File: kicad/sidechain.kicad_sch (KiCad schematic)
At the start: 30 parts, among them SW2 INT/EXT, SW3 HPF DEFEAT, SW4 LINK, U3 NE5532, U4 NE5532, U6 NE5532

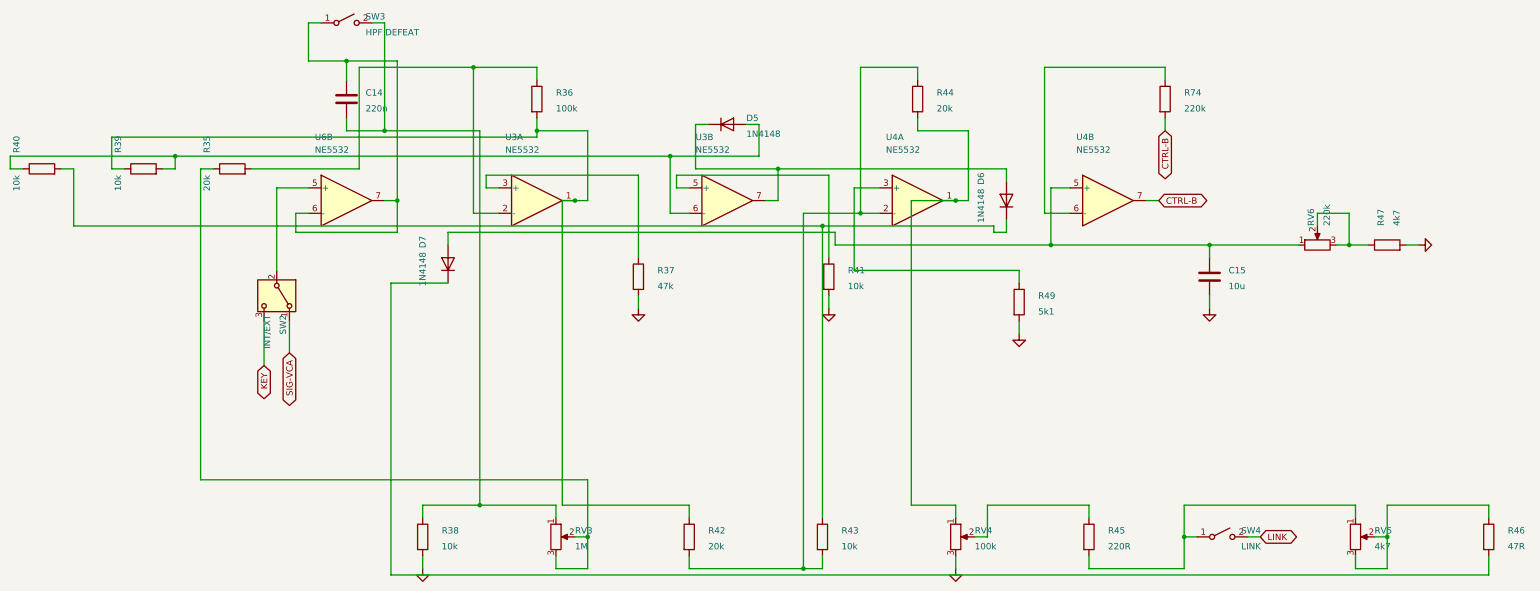
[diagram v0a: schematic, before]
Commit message: Add power shtuff and meters to big boy schematic
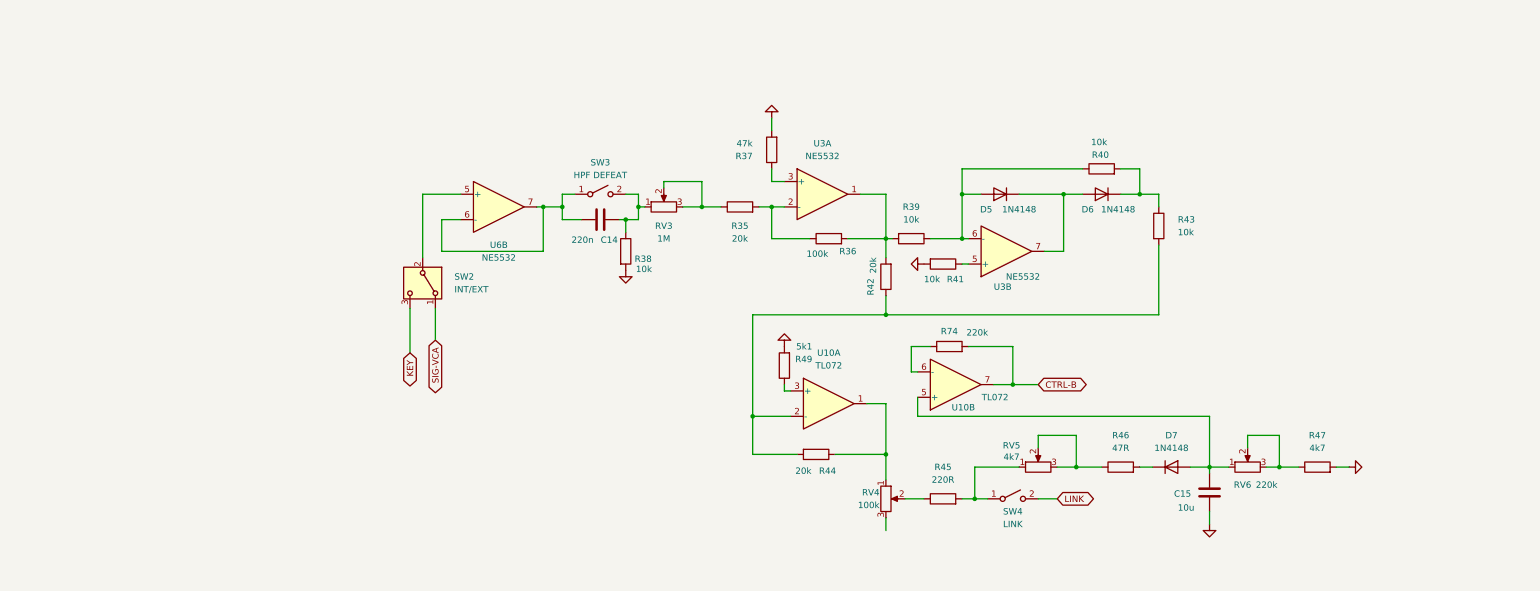
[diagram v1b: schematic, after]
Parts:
- removed U4: NE5532, Package_DIP:DIP-8_W7.62mm, symbol Amplifier_Operational:NE5532
- added U10: TL072, Package_DIP:DIP-8_W7.62mm, symbol Amplifier_Operational:NE5532
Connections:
- net AGND: no longer RV4.3
- net CTRL-B: now also U10.7
- net at C15.1, D7.2 (A), RV6.1: now also U10.5 (+)
- net at R49.1: now also U10.3 (+)
- net at R36.2, U3.1: now also R39.2, R42.2; no longer R39.1, R42.1
- net at R74.1: now also U10.6 (-)
- net at RV4.1: now also R44.1, U10.1; no longer R44.2
- net at D5.2 (A), R40.1, U3.6 (-): now also R39.1; no longer R39.2
- new net: R42.1, R43.2, R44.2, U10.2 (-)

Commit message: Add reorganised schematic to split files.
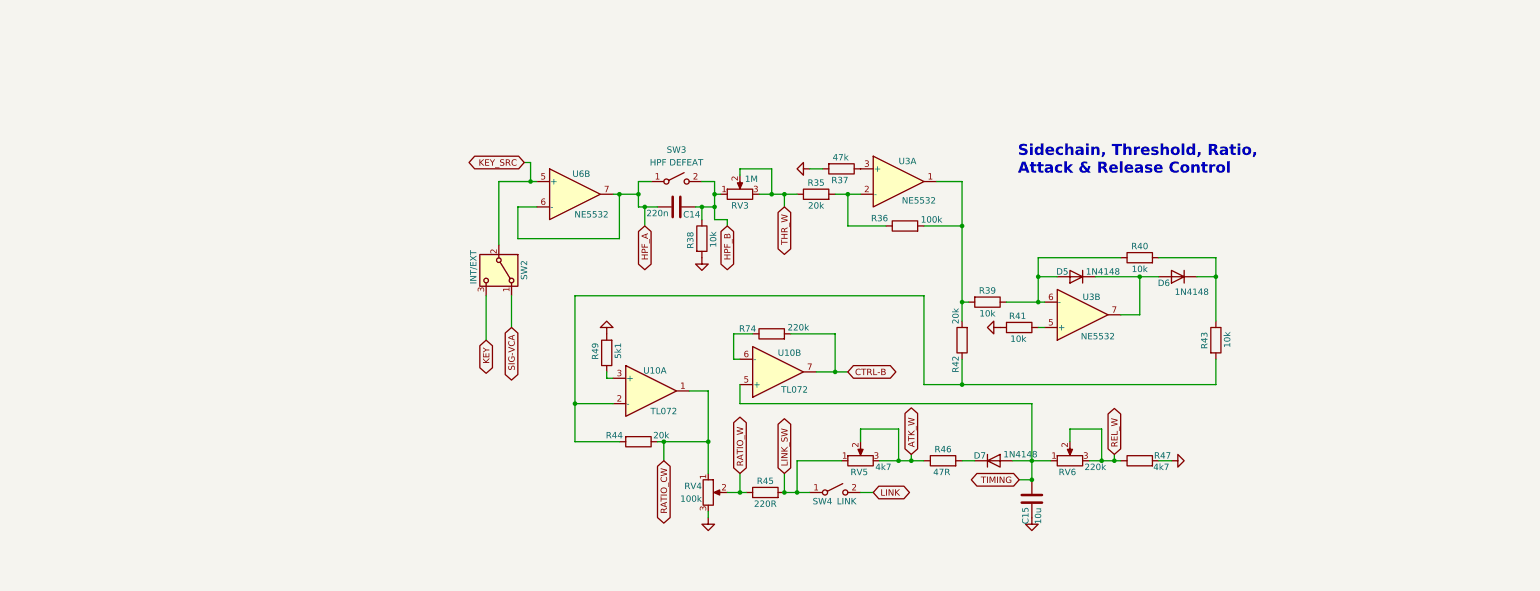
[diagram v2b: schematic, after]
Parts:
- RV3, RV4, RV5, RV6: now left out of the parts list
- SW2: footprint (none) -> Connector_PinHeader_2.54mm:PinHeader_1x03_P2.54mm_Vertical; now left out of the parts list
- SW3, SW4: footprint (none) -> Connector_PinHeader_2.54mm:PinHeader_1x02_P2.54mm_Vertical; now left out of the parts list
- U10, U3, U6: footprint Package_DIP:DIP-8_W7.62mm -> Package_DIP:DIP-8_W7.62mm_Socket
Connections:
- net AGND: now also RV4.3
- net KEY_SRC: now reaches SW2.2 (B), U6.5 (+)
- net HPF_A: now reaches C14.1, SW3.1 (A), U6.6 (-), U6.7
- net HPF_B: now reaches C14.2, R38.1, RV3.1, SW3.2 (B)
- net THR_W: now reaches R35.1, RV3.2, RV3.3
- net LINK_SW: now reaches R45.2, RV5.1, SW4.1 (A)
- net RATIO_CW: now reaches R44.1, RV4.1, U10.1
- net RATIO_W: now reaches R45.1, RV4.2
- net ATK_W: now reaches R46.1, RV5.2, RV5.3
- net TIMING: now reaches C15.1, D7.2 (A), RV6.1, U10.5 (+)
- net REL_W: now reaches R47.1, RV6.2, RV6.3
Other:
- note added: "Sidechain, Threshold, Ratio, Attack & Release Control"

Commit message: Match the split sheets' chip references to the board (#4)
Pasting the board schematic into the split sheets renumbered five units:
the VCA recovery amp was U4B (board U1B), the sidechain TL072 was U10
(board U4), U4's power unit was U10, U7's power unit was U11, and the
LM3915 was U12 (board U10). They now carry the board's references, so
the split sheets and compressor_with_pcb have the same 167 parts and the
same 119 nets.
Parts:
- renumbered U10 to U4
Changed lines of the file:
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@@
 		(in_pos_files yes)
 		(dnp no)
-		(property "Reference" "U10"
+		(property "Reference" "U4"
 			(at 182.626 95.25 0)
 			(show_name no)
@@
 			(project "UTS Mini Mixing Desk - Compressor"
 				(path "/fdeae63a-37f5-58fb-b342-cb68d8a6bfbc/726d8415-a5fc-52c7-823f-9ededf5a8991"
-					(reference "U10")
+					(reference "U4")
 					(unit 2)
 				)
@@
 		(in_pos_files yes)
 		(dnp no)
-		(property "Reference" "U10"
+		(property "Reference" "U4"
 			(at 155.702 98.806 0)
 			(show_name no)
@@
 			(project "UTS Mini Mixing Desk - Compressor"
 				(path "/fdeae63a-37f5-58fb-b342-cb68d8a6bfbc/726d8415-a5fc-52c7-823f-9ededf5a8991"
-					(reference "U10")
-					(unit 1)
-				)
+					(reference "U4")
+					(unit 1)
+				)

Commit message: Bring the compressor's values in line with the design targets
Through gain: R21/R22 3k3 to 6k8 halves the recovery amp's gain, so the
module is unity balanced in to out and BYPASS matches; R36 100k to 200k
keeps the detector's level. Bass: C9/C10 2u2 to 4u7 with the larger
input resistors puts the -3 dB point near 5 Hz.
Threshold: RV3 1M linear to 250k audio taper and R35 20k to 2k4 spread
about -20 to +20 dBu over the knob. R60 47k to 24k sets the resting
steer near 150 mV.
Timing: R45/R46/RV5 and R47/RV6/R74 scaled up to match the RC targets
with the same C15.

Same changes on the sheets, both boards and design.py. The simulation's
pot model gains an audio taper, and the burst test now runs at half
threshold.
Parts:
- R35: value 20k -> 2k4
- R36: value 100k -> 200k
- R45: value 220R -> 680R
- R46: value 47R -> 150R
- R47: value 4k7 -> 12k
- R74, RV6: value 220k -> 1M
- RV3: value 1M -> 250kA
- RV5: value 4k7 -> 20k
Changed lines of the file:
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@@
 			)
 		)
-		(property "Value" "4k7"
+		(property "Value" "12k"
 			(at 257.048 118.11 90)
 			(show_name no)
@@
 			)
 		)
-		(property "Value" "220R"
+		(property "Value" "680R"
 			(at 177.8 125.476 90)
 			(show_name no)
@@
 			)
 		)
-		(property "Value" "20k"
+		(property "Value" "2k4"
 			(at 187.96 65.786 90)
 			(show_name no)
@@
 			)
 		)
-		(property "Value" "47R"
+		(property "Value" "150R"
 			(at 213.106 119.126 90)
 			(show_name no)
@@
 			)
 		)
-		(property "Value" "220k"
+		(property "Value" "1M"
 			(at 184.404 90.17 90)
 			(show_name no)
@@
 			)
 		)
-		(property "Value" "1M"
+		(property "Value" "250kA"
 			(at 175.006 60.452 90)
 			(show_name no)
@@
 			)
 		)
-		(property "Sim.Params" "R=1e+06 POS={THRESHOLD}"
+		(property "Sim.Params" "R=250000 POS={THRESHOLD} TAPER=1"
 			(at 172.72 63.5 90)
 			(show_name no)
@@
 			)
 		)
-		(property "Value" "4k7"
+		(property "Value" "20k"
 			(at 201.422 118.11 90)
 			(show_name no)
@@
 			)
 		)
-		(property "Sim.Params" "R=4700 POS={ATTACK}"
+		(property "Sim.Params" "R=20000 POS={ATTACK}"
 			(at 196.85 116.84 90)
 			(show_name no)
@@
 			)
 		)
-		(property "Value" "220k"
+		(property "Value" "1M"
 			(at 243.84 118.11 90)
 			(show_name no)
@@
 			)
 		)
-		(property "Sim.Params" "R=220000 POS={RELEASE}"
+		(property "Sim.Params" "R=1e+06 POS={RELEASE}"
 			(at 238.76 116.84 90)
 			(show_name no)
@@
 			)
 		)
-		(property "Value" "100k"
+		(property "Value" "200k"
 			(at 211.074 68.58 90)
 			(show_name no)

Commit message: Retune attack and release: R45 220R, R46 47R, RV5 10k, R47 15k
The first pass ran the attack too slow (9 to 103 ms against a 2.7 to
50 ms target). Results are regenerated in the next commit.
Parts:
- R45: value 680R -> 220R
- R46: value 150R -> 47R
- R47: value 12k -> 15k
- RV5: value 20k -> 10k
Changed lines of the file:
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@@
 			)
 		)
-		(property "Value" "12k"
+		(property "Value" "15k"
 			(at 257.048 118.11 90)
 			(show_name no)
@@
 			)
 		)
-		(property "Value" "680R"
+		(property "Value" "220R"
 			(at 177.8 125.476 90)
 			(show_name no)
@@
 			)
 		)
-		(property "Value" "150R"
+		(property "Value" "47R"
 			(at 213.106 119.126 90)
 			(show_name no)
@@
 			)
 		)
-		(property "Value" "20k"
+		(property "Value" "10k"
 			(at 201.422 118.11 90)
 			(show_name no)
@@
 			)
 		)
-		(property "Sim.Params" "R=20000 POS={ATTACK}"
+		(property "Sim.Params" "R=10000 POS={ATTACK}"
 			(at 196.85 116.84 90)
 			(show_name no)

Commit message: Stop the fast-attack overshoot: C22 47u to 4u7
C22 made STA lag STB by about 60 ms, so when CTRL-B pulled the
reference node down the steering kept moving after the control
voltage had settled, overshooting by up to 20 dB. With 4u7 the two
sides track and the overshoot is about 1 dB. RV5 back to 4k7 and RV6
to 500k, since the attack and release run slower without it.
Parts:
- RV5: value 10k -> 4k7
- RV6: value 1M -> 500k
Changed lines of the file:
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@@
 			)
 		)
-		(property "Value" "10k"
+		(property "Value" "4k7"
 			(at 201.422 118.11 90)
 			(show_name no)
@@
 			)
 		)
-		(property "Sim.Params" "R=10000 POS={ATTACK}"
+		(property "Sim.Params" "R=4700 POS={ATTACK}"
 			(at 196.85 116.84 90)
 			(show_name no)
@@
 			)
 		)
-		(property "Value" "1M"
+		(property "Value" "500k"
 			(at 243.84 118.11 90)
 			(show_name no)
@@
 			)
 		)
-		(property "Sim.Params" "R=1e+06 POS={RELEASE}"
+		(property "Sim.Params" "R=500000 POS={RELEASE}"
 			(at 238.76 116.84 90)
 			(show_name no)

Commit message: Keep R74 at 220k and write up the new results
R74 at 1M only moved CTRL-B's resting offset further from zero with an
NE5532 in U4, so it goes back to 220k. The sim README now lists the
eleven changed values with before, after and target figures.
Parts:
- R74: value 1M -> 220k
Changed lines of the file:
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@@
 			)
 		)
-		(property "Value" "1M"
+		(property "Value" "220k"
 			(at 184.404 90.17 90)
 			(show_name no)
